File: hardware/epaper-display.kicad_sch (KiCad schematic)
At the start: 48 parts, among them J1 AES200200A00 FPC, J2 USB-C, J3 LiPo JST-PH, J4 I2C temp (optional), J5 UART, J6 GPIO expansion, Q1 Si1304BDL / NX3008NBK, SW1 EN/RESET, SW2 BOOT, U1 ESP32-S3-WROOM-1, U2 MCP73831T-2ACI/OT, U3 MCP1825S-3302E/DB

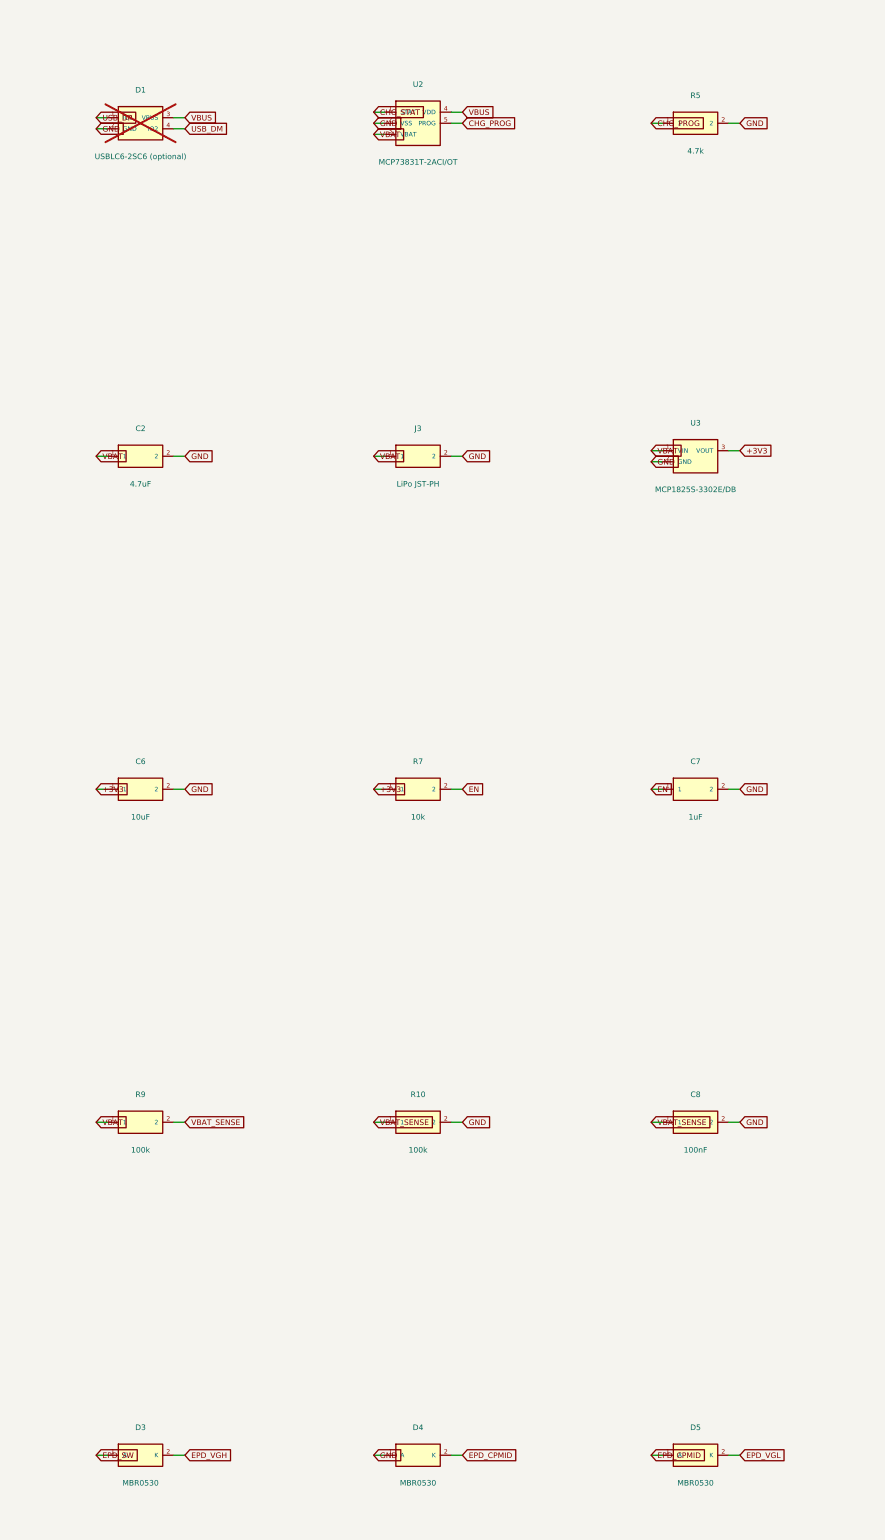
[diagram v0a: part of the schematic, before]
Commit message: Fix charge-pump diode orientation, sheet overflow, USB symbol/footprint mismatch
Co-Authored-By: Devin AI <158243242+devin-ai-integration[bot]@users.noreply.github.com>
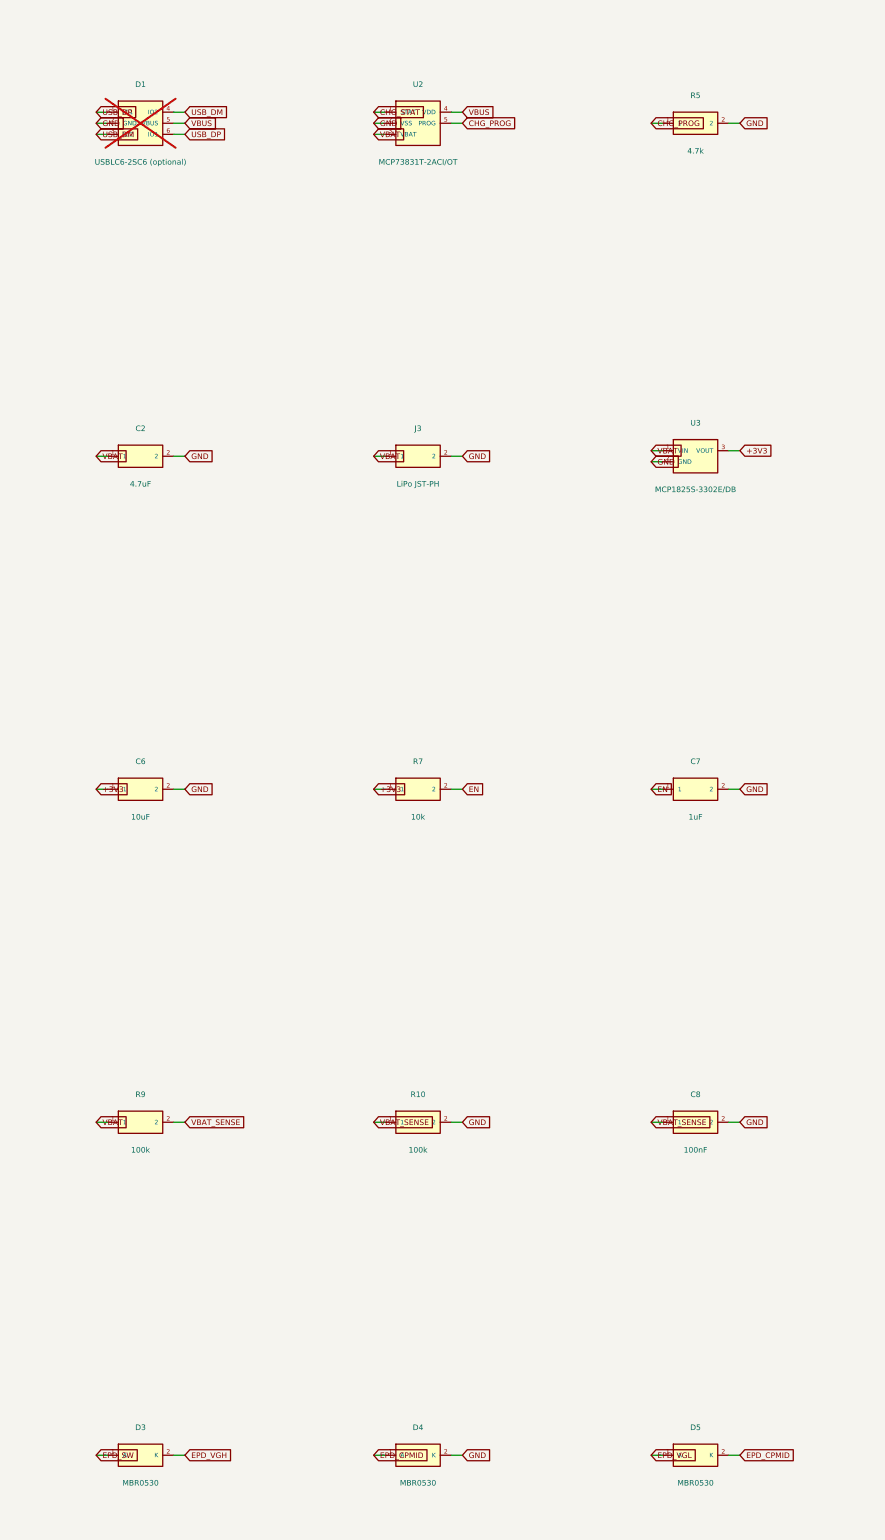
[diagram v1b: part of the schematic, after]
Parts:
- J2: footprint Connector_USB:USB_C_Receptacle_GCT_USB4085 -> (none)
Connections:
- net EPD_CPMID: now also D4.1 (A), D5.2 (K); no longer D4.2 (K), D5.1 (A)
- net EPD_VGL: now also D5.1 (A); no longer D5.2 (K)
- net GND: now also D4.2 (K); no longer D4.1 (A)
- net USB_DM: now also D1.3 (IO2)
- net USB_DP: now also D1.6 (IO1)
- net VBUS: now also D1.5 (VBUS); no longer D1.3 (VBUS)

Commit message: hardware: assign footprints to every BOM component, shape labels by pin type
Co-Authored-By: Devin AI <158243242+devin-ai-integration[bot]@users.noreply.github.com>
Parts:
- C1, C2, C3, C4, C6: footprint (none) -> Capacitor_SMD:C_0805_2012Metric
- C10, C11, C12, C13, C14, C15, C16, C17, C5, C7, C8, C9: footprint (none) -> Capacitor_SMD:C_0603_1608Metric
- D3, D4, D5: footprint (none) -> Diode_SMD:D_SOD-123
- J2: footprint (none) -> Connector_USB:USB_C_Receptacle_GCT_USB4085
- L1: footprint (none) -> Inductor_SMD:L_1210_3225Metric
- R1, R10, R11, R12, R13, R2, R3, R4, R5, R6, R7, R8, R9: footprint (none) -> Resistor_SMD:R_0603_1608Metric

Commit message: hardware: keep chip passives at 0805 for hand assembly
Co-Authored-By: Devin AI <158243242+devin-ai-integration[bot]@users.noreply.github.com>
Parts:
- C10, C11, C12, C13, C14, C15, C16, C17, C5, C7, C8, C9: footprint Capacitor_SMD:C_0603_1608Metric -> Capacitor_SMD:C_0805_2012Metric
- R1, R10, R11, R12, R13, R2, R3, R4, R5, R6, R7, R8, R9: footprint Resistor_SMD:R_0603_1608Metric -> Resistor_SMD:R_0805_2012Metric

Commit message: hardware: apply ESP32-S3 pin review fixes
Co-Authored-By: Devin AI <158243242+devin-ai-integration[bot]@users.noreply.github.com>
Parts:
- added R14: 10k, Resistor_SMD:R_0805_2012Metric, symbol epaper:R
- added R15: 10k (DNP), Resistor_SMD:R_0805_2012Metric, symbol epaper:R
- U1: value ESP32-S3-WROOM-1 -> ESP32-S3-WROOM-1-N8
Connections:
- net +3V3: now also R14.1
- net EPD_CS: now also R14.2
- net GND: now also R15.2
- net STRAP_IO3: now reaches U1.15 (IO3)
- net STRAP_IO3: now also R15.1
- no-connect marks 5 -> 4
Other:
- note added: "J6 IO35-37 and IO47/48 assume non-octal-PSRAM, non-R16V module"

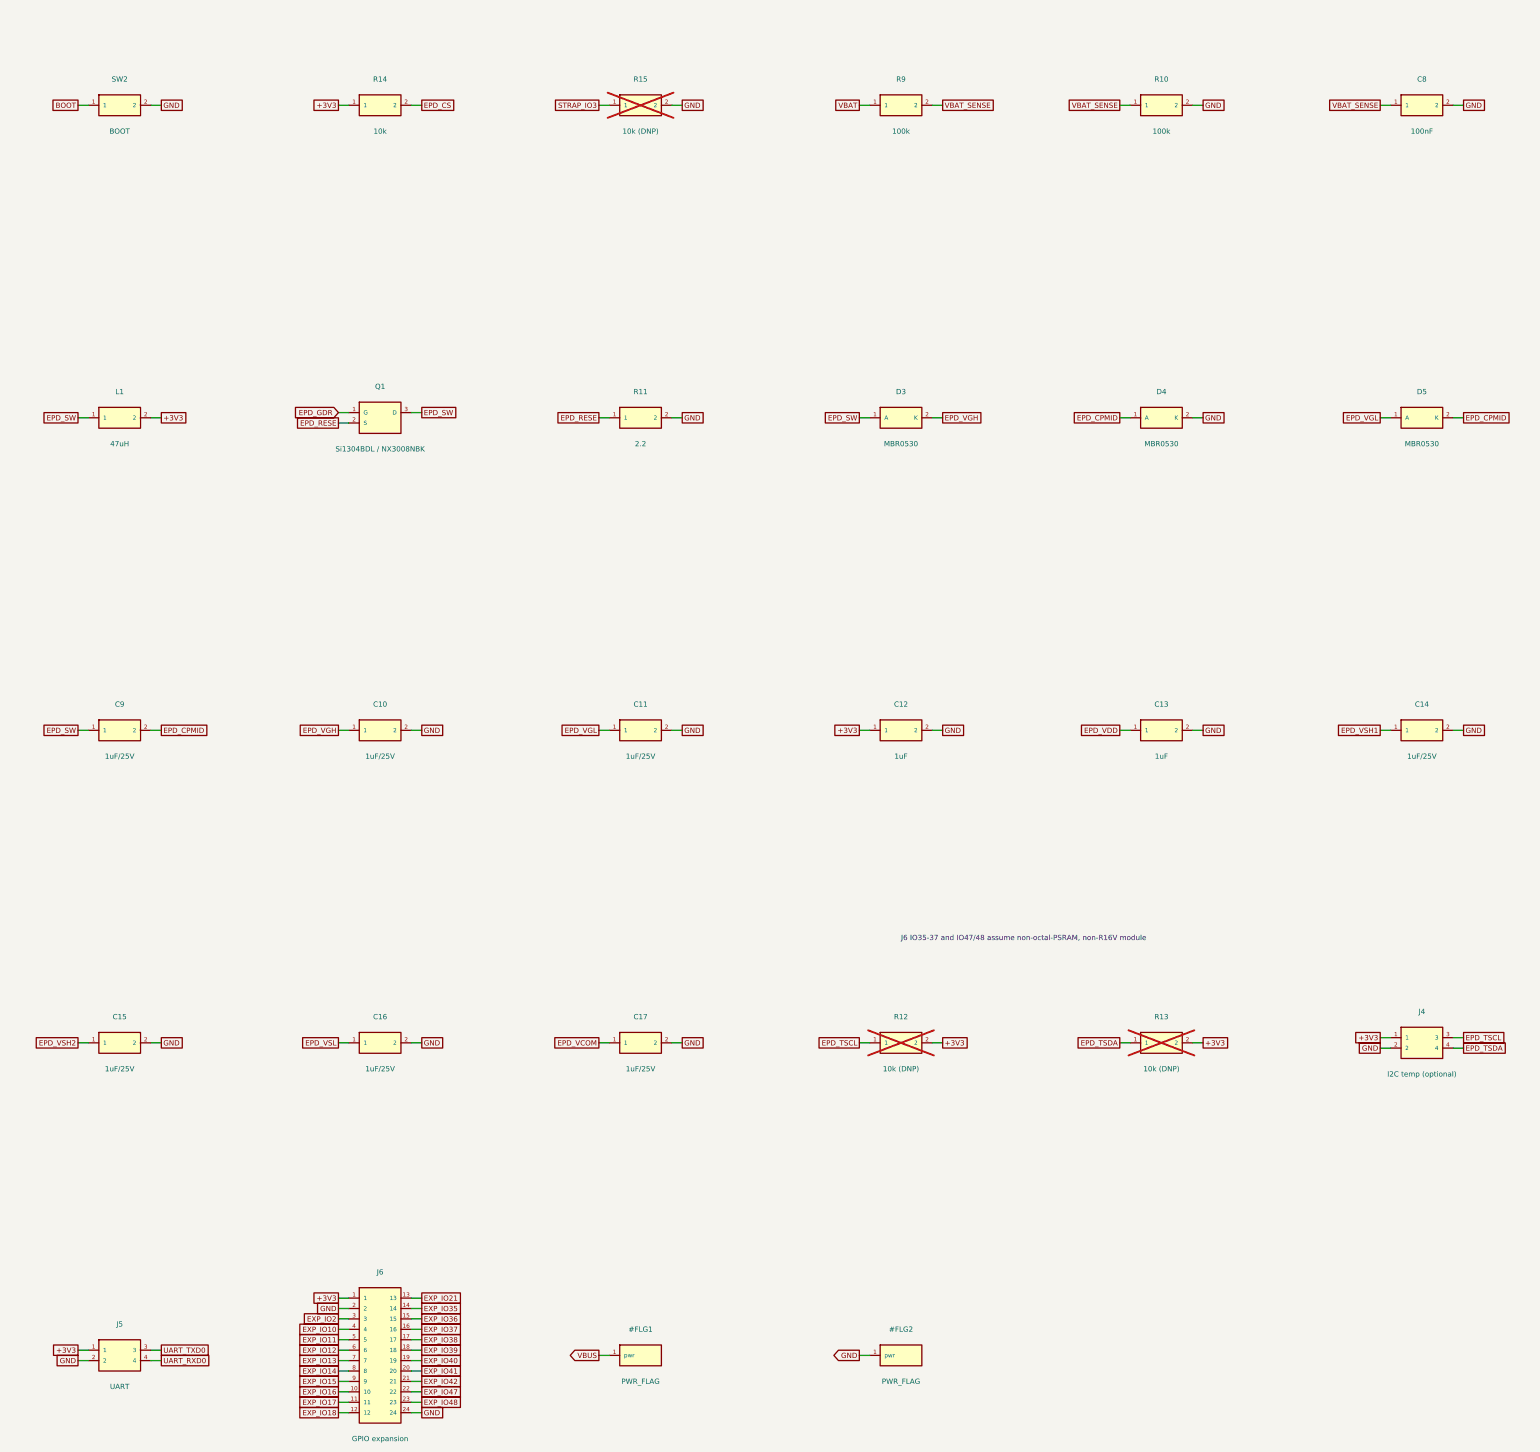
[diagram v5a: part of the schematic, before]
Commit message: hardware: hold e-paper panel in reset
Co-Authored-By: Devin AI <158243242+devin-ai-integration[bot]@users.noreply.github.com>
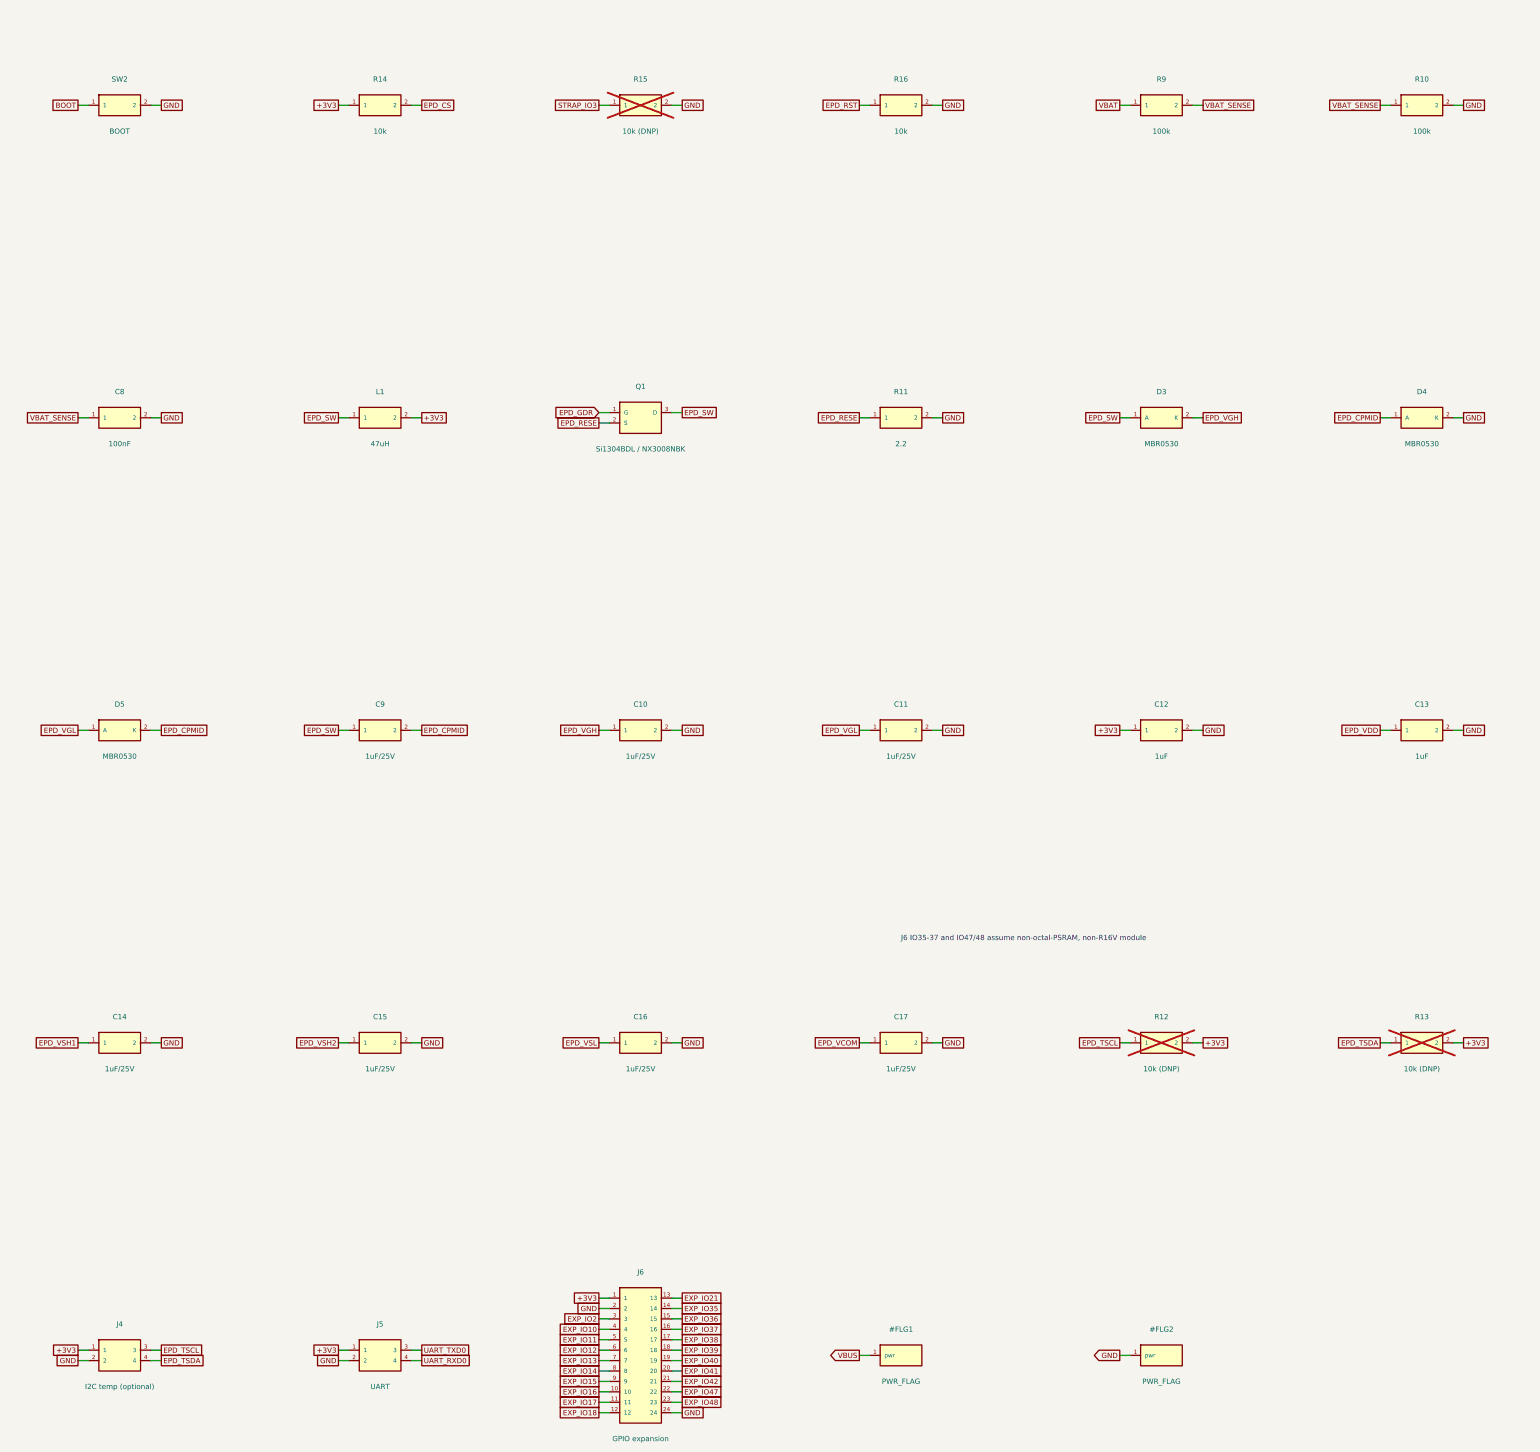
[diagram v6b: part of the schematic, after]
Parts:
- added R16: 10k, Resistor_SMD:R_0805_2012Metric, symbol epaper:R
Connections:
- net EPD_RST: now also R16.1
- net GND: now also R16.2
